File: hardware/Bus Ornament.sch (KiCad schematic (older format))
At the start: 26 parts, among them J1 Conn_02x03_Odd_Even, SW1 SW_SPST, SW2 SW_Push, U1 ATtiny85-20PU, U2 TPS62203DBV

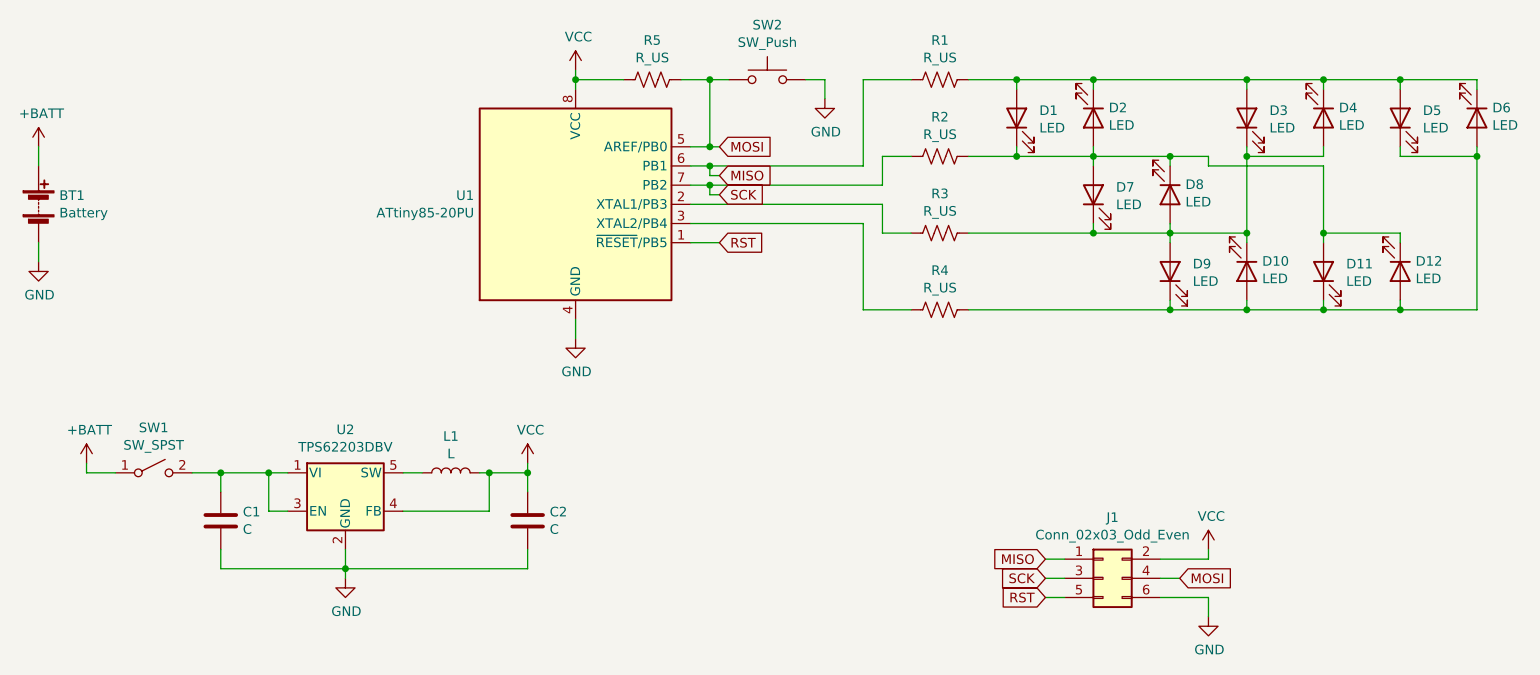
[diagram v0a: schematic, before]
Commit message: Firmware written but untested
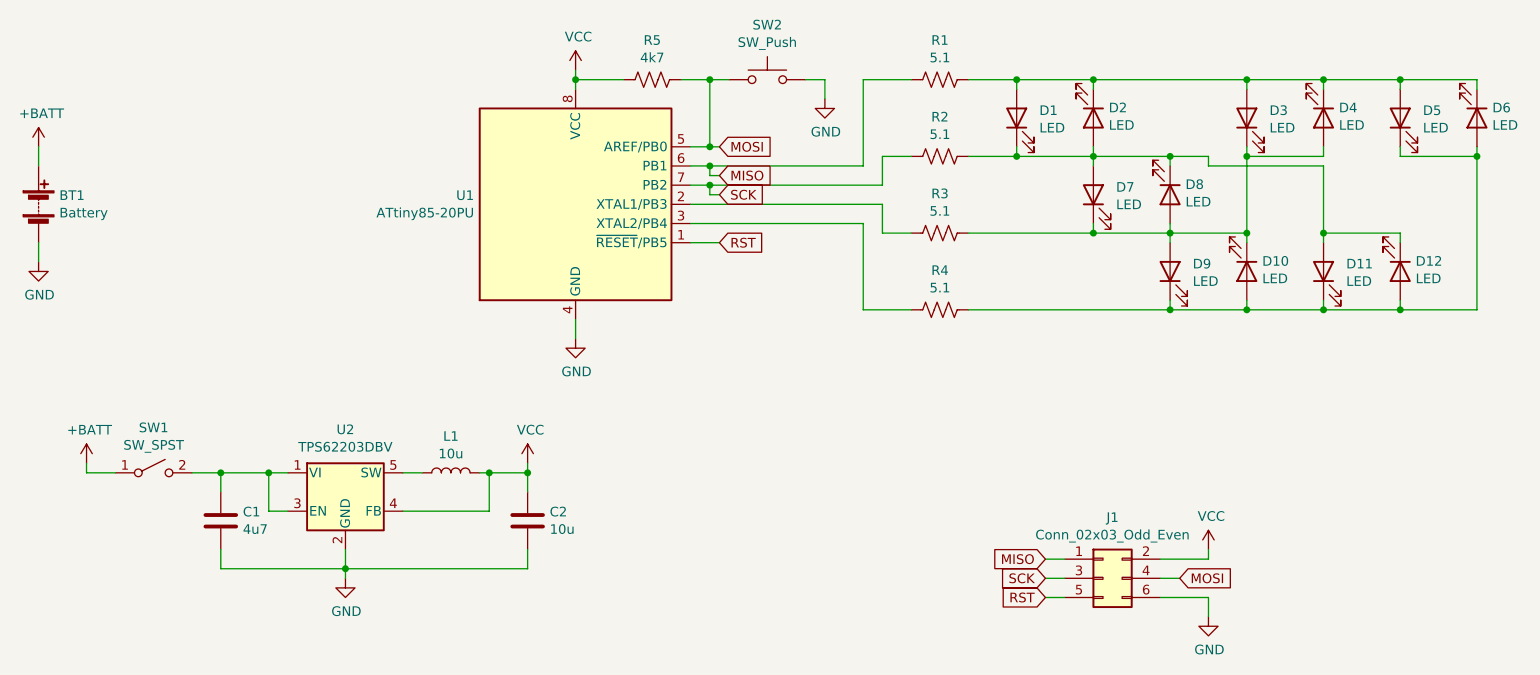
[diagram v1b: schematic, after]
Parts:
- C1: value C -> 4u7
- C2: value C -> 10u
- L1: value L -> 10u
- R1, R2, R3, R4: value R_US -> 5.1
- R5: value R_US -> 4k7
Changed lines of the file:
@@
 P 5900 1550
 F 0 "R1" V 5695 1550 50  0000 C CNN
-F 1 "R_US" V 5786 1550 50  0000 C CNN
+F 1 "5.1" V 5786 1550 50  0000 C CNN
 F 2 "Resistor_SMD:R_1206_3216Metric" V 5940 1540 50  0001 C CNN
 F 3 "~" H 5900 1550 50  0001 C CNN
@@
 P 5900 1950
 F 0 "R2" V 5695 1950 50  0000 C CNN
-F 1 "R_US" V 5786 1950 50  0000 C CNN
+F 1 "5.1" V 5786 1950 50  0000 C CNN
 F 2 "Resistor_SMD:R_1206_3216Metric" V 5940 1940 50  0001 C CNN
 F 3 "~" H 5900 1950 50  0001 C CNN
@@
 P 5900 2350
 F 0 "R3" V 5695 2350 50  0000 C CNN
-F 1 "R_US" V 5786 2350 50  0000 C CNN
+F 1 "5.1" V 5786 2350 50  0000 C CNN
 F 2 "Resistor_SMD:R_1206_3216Metric" V 5940 2340 50  0001 C CNN
 F 3 "~" H 5900 2350 50  0001 C CNN
@@
 P 5900 2750
 F 0 "R4" V 5695 2750 50  0000 C CNN
-F 1 "R_US" V 5786 2750 50  0000 C CNN
+F 1 "5.1" V 5786 2750 50  0000 C CNN
 F 2 "Resistor_SMD:R_1206_3216Metric" V 5940 2740 50  0001 C CNN
 F 3 "~" H 5900 2750 50  0001 C CNN
@@
 P 4400 1550
 F 0 "R5" V 4195 1550 50  0000 C CNN
-F 1 "R_US" V 4286 1550 50  0000 C CNN
+F 1 "4k7" V 4286 1550 50  0000 C CNN
 F 2 "Resistor_SMD:R_1206_3216Metric" V 4440 1540 50  0001 C CNN
 F 3 "~" H 4400 1550 50  0001 C CNN
@@
 P 2150 3850
 F 0 "C1" H 2265 3896 50  0000 L CNN
-F 1 "C" H 2265 3805 50  0000 L CNN
+F 1 "4u7" H 2265 3805 50  0000 L CNN
 F 2 "Capacitor_SMD:C_1206_3216Metric" H 2188 3700 50  0001 C CNN
 F 3 "~" H 2150 3850 50  0001 C CNN
@@
 P 3750 3850
 F 0 "C2" H 3865 3896 50  0000 L CNN
-F 1 "C" H 3865 3805 50  0000 L CNN
+F 1 "10u" H 3865 3805 50  0000 L CNN
 F 2 "Capacitor_SMD:C_1206_3216Metric" H 3788 3700 50  0001 C CNN
 F 3 "~" H 3750 3850 50  0001 C CNN
@@
 P 3350 3600
 F 0 "L1" V 3540 3600 50  0000 C CNN
-F 1 "L" V 3449 3600 50  0000 C CNN
+F 1 "10u" V 3449 3600 50  0000 C CNN
 F 2 "Inductor_SMD:L_Coilcraft_XAL60xx_6.36x6.56mm" H 3350 3600 50  0001 C CNN
 F 3 "~" H 3350 3600 50  0001 C CNN
